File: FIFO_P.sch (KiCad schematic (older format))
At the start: 50 parts, among them J1 Vin +, J2 Vin -, J3 ICLK, J4 Vout, SW1 Rotary_Encoder_61C, U1 SN74LVC2G157_MUX_TI, U10 AD7840, U2 IDT_ICS551, U3 LTC1740, U4 ARDUINO_DUE_FIFO_P_COMMANDS, U5 IDT_72V2105, U6 TXB0104, U7 TXB0104, U8 TXB0104, U9 TXB0104

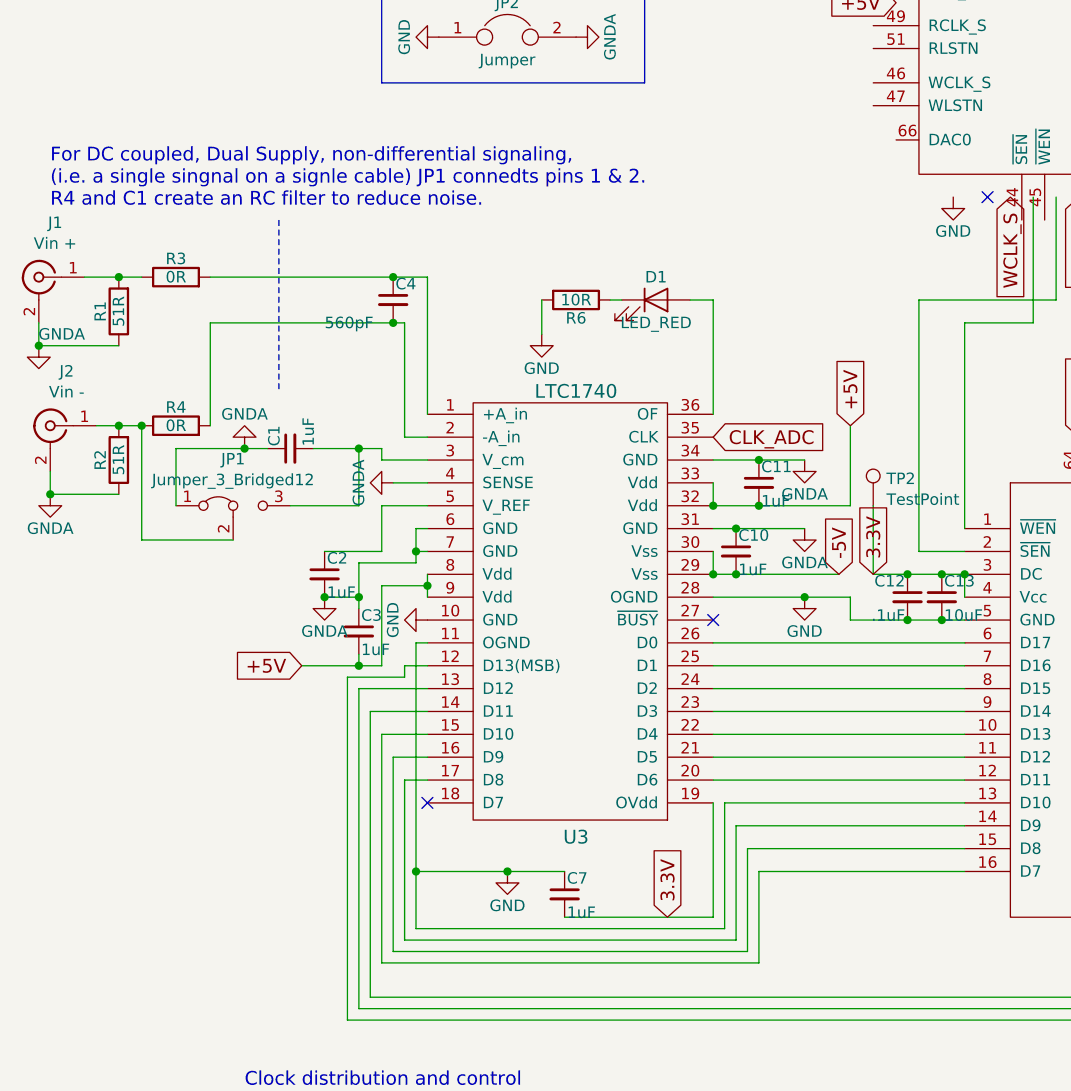
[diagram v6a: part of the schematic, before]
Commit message: Fixed FIFO pin
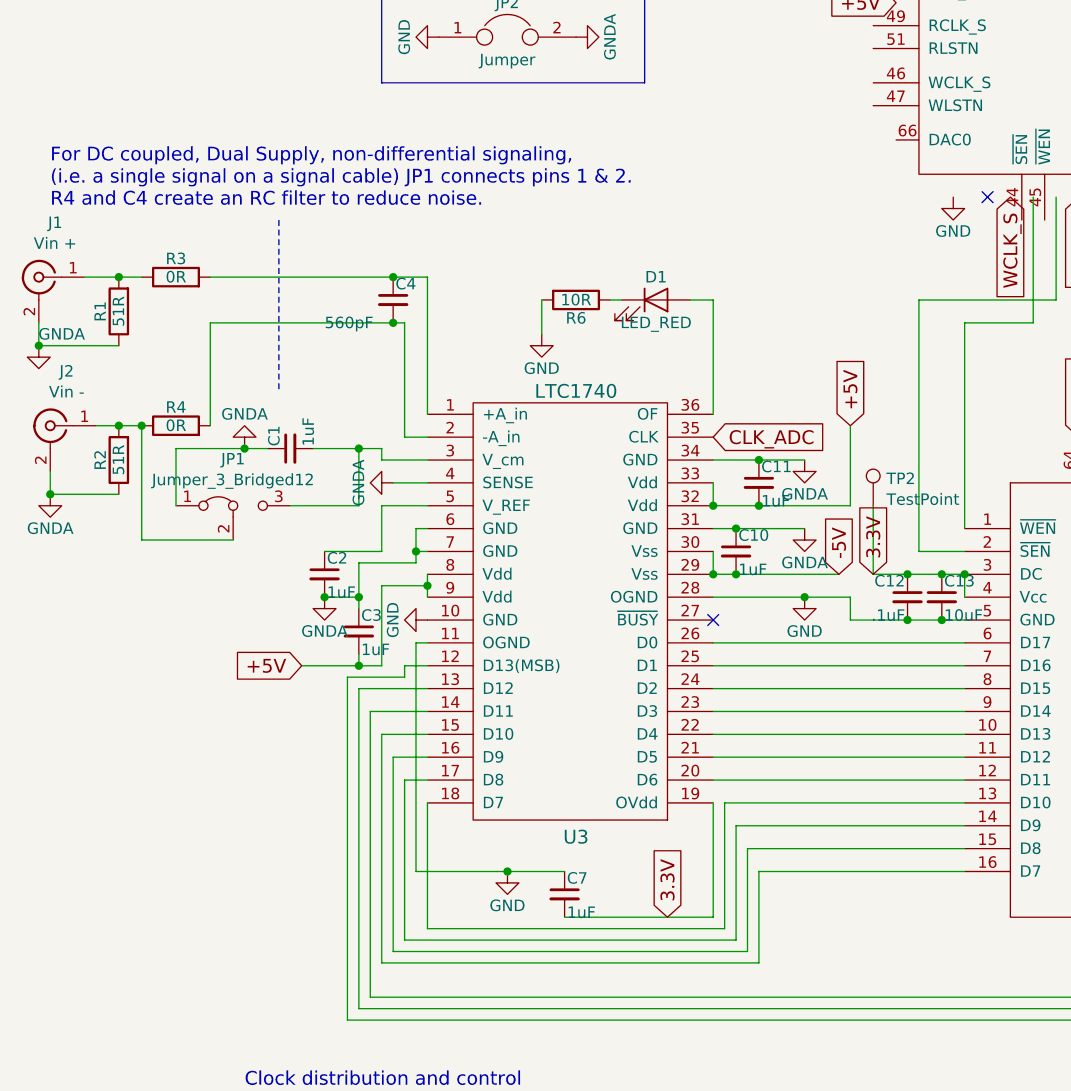
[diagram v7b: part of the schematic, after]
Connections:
- no-connect marks 30 -> 29
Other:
- note added: "For DC coupled, Dual Supply, non-differential signaling,\n(i.e. a single signal on a signal cable) JP1 connects pins 1 & 2.\nR4 and C4 create an RC filter to reduce noise."
- note removed: "For DC coupled, Dual Supply, non-differential signaling,\n(i.e. a single singnal on a signle cable) JP1 connedts pins 1 & 2.\nR4 and C1 create an RC filter to reduce noise."
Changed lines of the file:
@@
 $EndDescr
-$Comp
-L FIFO_P:LTC1740 U3
-U 1 1 592106E2
-P 2100 2850
-F 0 "U3" H 2750 1000 60  0000 C CNN
-F 1 "LTC1740" H 2750 2950 60  0000 C CNN
-F 2 "FIFO_P:SSOP-36_5.3mm_Pitch0.65mm" H 2700 2050 60  0001 C CNN
-F 3 "" H 2700 2050 60  0000 C CNN
-	1    2100 2850
-	1    0    0    -1
-$EndComp
 $Comp
 L Device:R R1
@@
 Connection ~ 750  2900
 Wire Wire Line
-	2100 2250 2100 2850
-Wire Wire Line
 	1150 2450 1950 2450
 Wire Wire Line
@@
 	3350 3250 3550 3250
 Wire Wire Line
-	3350 2350 3350 2850
-Wire Wire Line
 	3350 5050 3350 4550
 Wire Wire Line
@@
 Wire Wire Line
 	3350 4450 4450 4450
-Wire Wire Line
-	2050 5100 3400 5100
 Wire Wire Line
 	3400 5100 3400 4550
@@
 $EndSheet
 Text Notes 450  1950 0    60   ~ 0
-For DC coupled, Dual Supply, non-differential signaling,\n(i.e. a single singnal on a signle cable) JP1 connedts pins 1 & 2.\nR4 and C1 create an RC filter to reduce noise.
+For DC coupled, Dual Supply, non-differential signaling,\n(i.e. a single signal on a signal cable) JP1 connects pins 1 & 2.\nR4 and C4 create an RC filter to reduce noise.
 Wire Notes Line
 	1450 2000 1450 2750
@@
 NoConn ~ 5400 5250
 NoConn ~ 5500 5250
-NoConn ~ 2100 4550
-Connection ~ 3350 3250
-Connection ~ 3350 3550
-Wire Wire Line
-	2050 5100 2050 4850
 Wire Wire Line
 	2050 3850 2100 3850
-Connection ~ 2050 4850
-Wire Wire Line
-	2050 4850 2050 3850
 Wire Wire Line
 	2100 3350 2050 3350
@@
 	0    1    1    0
 $EndComp
+Connection ~ 3350 3550
+Connection ~ 3350 3250
+Wire Wire Line
+	3350 2350 3350 2850
+Wire Wire Line
+	2100 2250 2100 2850
+$Comp
+L FIFO_P:LTC1740 U3
+U 1 1 592106E2
+P 2100 2850
+F 0 "U3" H 2750 1000 60  0000 C CNN
+F 1 "LTC1740" H 2750 2950 60  0000 C CNN
+F 2 "FIFO_P:SSOP-36_5.3mm_Pitch0.65mm" H 2700 2050 60  0001 C CNN
+F 3 "" H 2700 2050 60  0000 C CNN
+	1    2100 2850
+	1    0    0    -1
+$EndComp
+Wire Wire Line
+	2100 4550 2100 5100
+Wire Wire Line
+	2100 5100 3400 5100
+Wire Wire Line
+	2050 4850 2050 3850
 $EndSCHEMATC

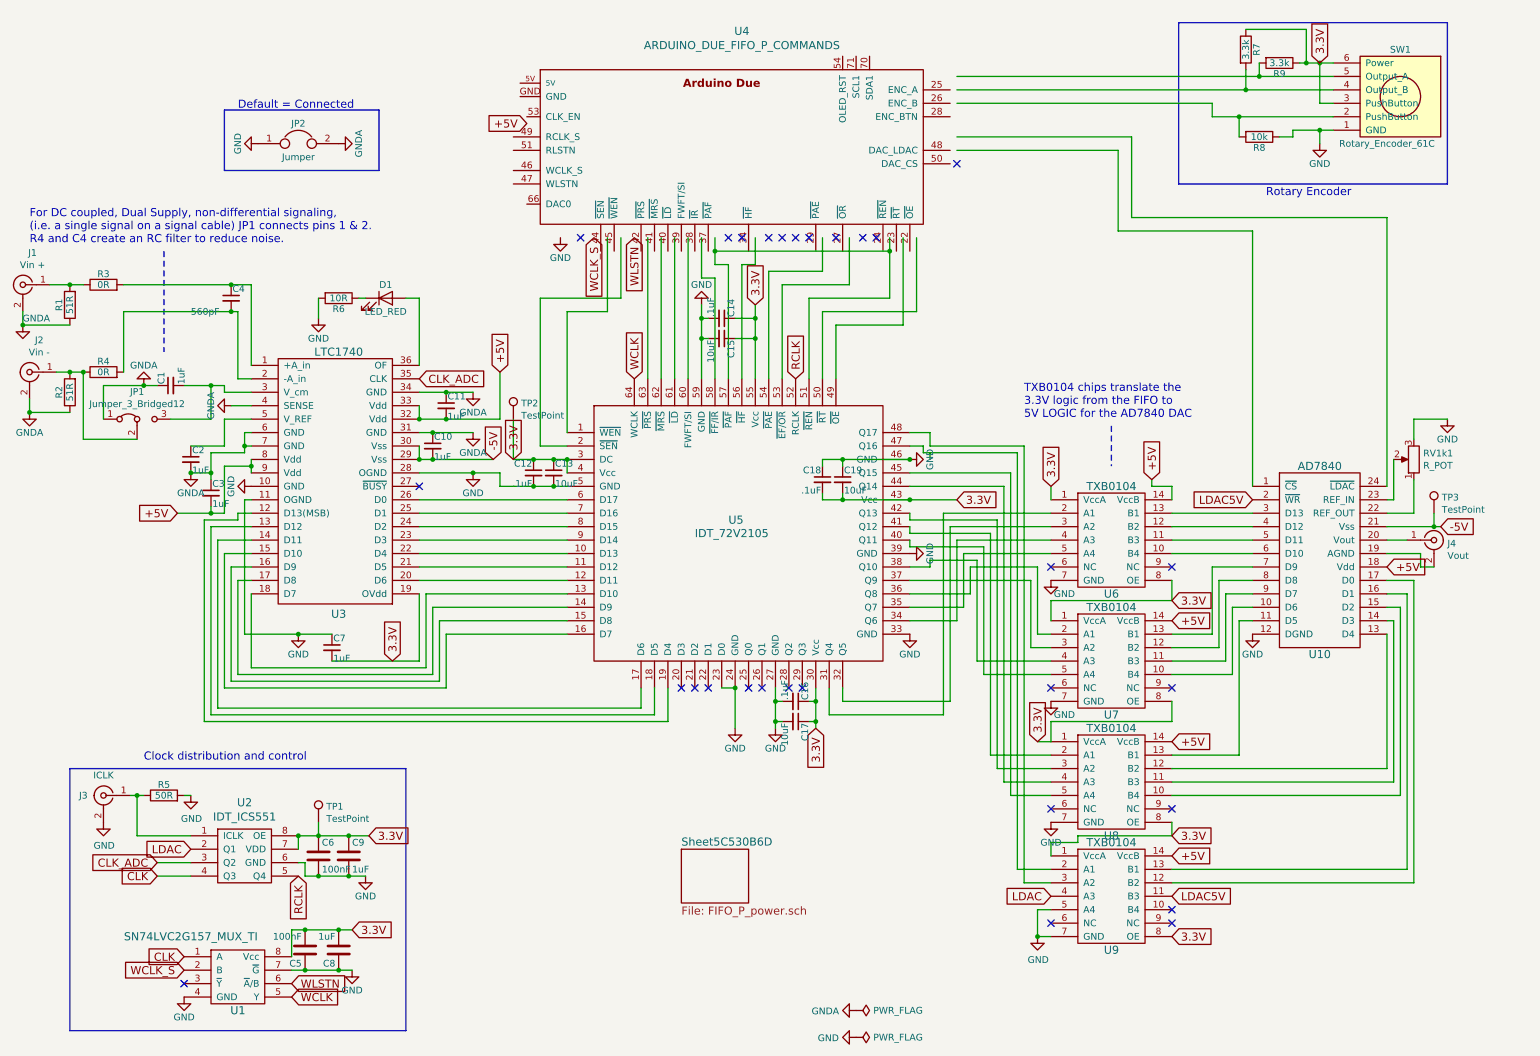
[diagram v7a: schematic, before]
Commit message: Begin cleaning up schematic. FIFO-DAC area ripped up
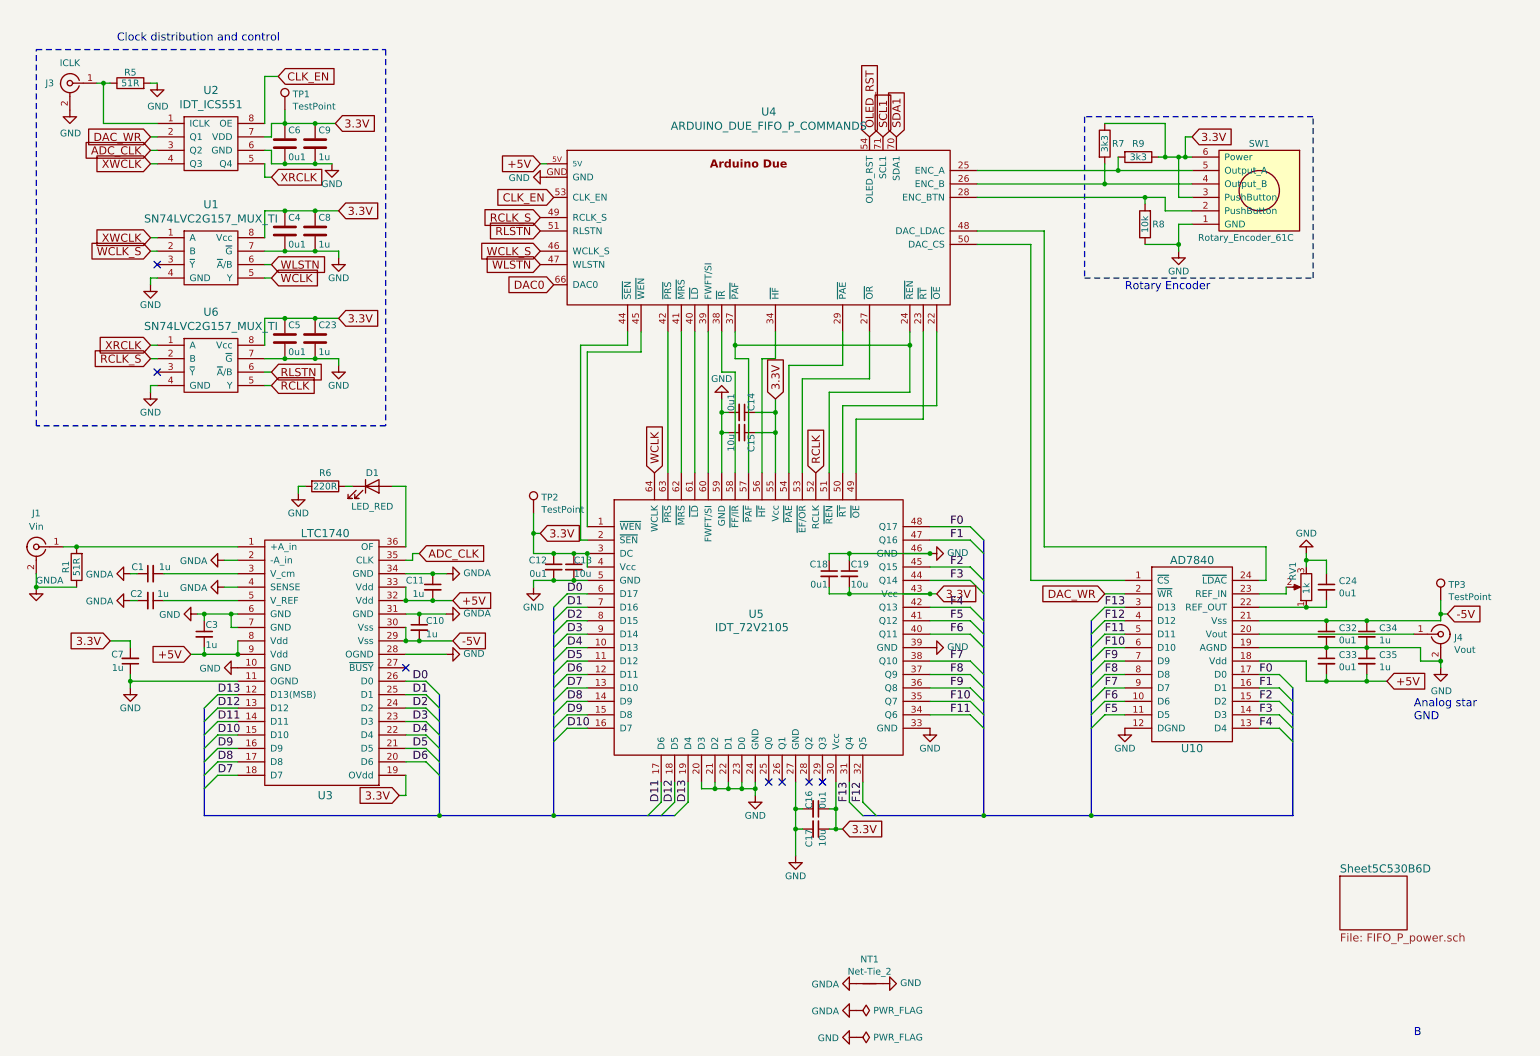
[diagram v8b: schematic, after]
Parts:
- removed C4: 560pF, Capacitor_THT:C_Rect_L4.0mm_W2.5mm_P2.50mm, symbol Device:C_Small
- removed J2: Vin -, Connector_Coaxial:BNC_TEConnectivity_1478204_Vertical, symbol Connector:Conn_Coaxial
- removed JP1: Jumper_3_Bridged12, Jumper:SolderJumper-3_P1.3mm_Open_RoundedPad1.0x1.5mm, symbol Jumper:Jumper_3_Bridged12
- removed JP2: Jumper, Connector_PinHeader_2.54mm:PinHeader_1x02_P2.54mm_Vertical, symbol Device:Jumper
- removed R2: 51R, Resistor_THT:R_Axial_DIN0204_L3.6mm_D1.6mm_P7.62mm_Horizontal, symbol Device:R
- removed R3, R4: 0R, Resistor_THT:R_Axial_DIN0204_L3.6mm_D1.6mm_P5.08mm_Horizontal, symbol Device:R
- removed U6, U7, U8, U9: TXB0104, Package_SO:TSSOP-14_4.4x5mm_P0.65mm, symbol FIFO_P:TXB0104
- added C23: 1u, Capacitor_THT:C_Rect_L4.0mm_W2.5mm_P2.50mm, symbol Device:C
- added C24, C32, C33: 0u1, symbol Device:C_Small
- added C34, C35: 1u, symbol Device:C_Small
- added C4: 0u1, Capacitor_THT:C_Rect_L4.0mm_W2.5mm_P2.50mm, symbol Device:C
- added NT1: Net-Tie_2, symbol Device:Net-Tie_2
- added U6: SN74LVC2G157_MUX_TI, symbol FIFO_P:SN74LVC2G157_MUX_TI
- C1, C10, C11, C2, C3, C7, C8, C9: value 1uF -> 1u
- C12, C14, C16, C18: value .1uF -> 0u1
- C13, C15, C17, C19: value 10uF -> 10u
- C5, C6: value 100nF -> 0u1
- J1: value Vin + -> Vin
- R5: value 50R -> 51R
- R6: value 10R -> 220R
- R7, R9: value 3.3k -> 3k3
- RV1: renamed from RV1k1; value R_POT -> 1k
- U1: footprint Package_SO:SSOP-8_2.95x2.8mm_P0.65mm -> (none)
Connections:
- net labels added: ADC_CLK, CLK_EN, D0, D1, D10, D11, D12, D13, D2, D3, D4, D5, D6, D7, D8, D9, DAC0, DAC_WR, F0, F1, F10, F11, F12, F13, F2, F3, F4, F5, F6, F7, F8, F9, OLED_RST, RCLK_S, RLSTN, SCL1, SDA1, XRCLK, XWCLK
- net labels removed: CLK, CLK_ADC, LDAC, LDAC5V
- wire segments 363 -> 305
- no-connect marks 29 -> 7
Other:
- note added: "Analog star\nGND"
- note added: "B"
- note removed: "Default = Connected"
- note removed: "For DC coupled, Dual Supply, non-differential signaling,\n(i.e. a single signal on a signal cable) JP1 connects pins 1 & 2.\nR4 and C4 create an RC filter to reduce noise."
- note removed: "TXB0104 chips translate the \n3.3V logic from the FIFO to \n5V LOGIC for the AD7840 DAC"
- moved on the sheet: C1, C10, C11, C12, C13, C14, C15, C16, C17, C18, C19, C2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
